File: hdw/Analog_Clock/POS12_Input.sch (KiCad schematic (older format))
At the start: 23 parts

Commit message: a few sch adjustments
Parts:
- removed C?: 0.1uF, Capacitors_SMD:C_0402, symbol Custom_Library:C_Custom
- removed R?: 6.04M, Resistors_SMD:R_0402, symbol Custom_Library:R_Custom
- removed R?: 86.6k, Resistors_SMD:R_0402, symbol Custom_Library:R_Custom
- removed R?: 243k, Resistors_SMD:R_0402, symbol Custom_Library:R_Custom
- removed R?: 100k, Resistors_SMD:R_0402, symbol Custom_Library:R_Custom
- removed R? (x4): 10, Resistors_SMD:R_0402, symbol Custom_Library:R_Custom
- removed R?: 5.1k, Resistors_SMD:R_0402, symbol Custom_Library:R_Custom
- removed R?: 13.7k, Resistors_SMD:R_0402, symbol Custom_Library:R_Custom
- removed R?: 0.02, Resistors_SMD:R_0612, symbol Custom_Library:R_Custom
- removed R?: 5.23k, Resistors_SMD:R_0402, symbol Custom_Library:R_Custom
- removed TP?: TP, Pin_Headers:Pin_Header_Angled_1x01_Pitch2.54mm, symbol Custom_Library:TP
- removed TP? (x2): TP, Custom Footprints Library:Test_Point, symbol Custom_Library:TP
- removed U?: LTC4365DDB, Housings_DFN_QFN:DFN-8-1EP_2x3mm_Pitch0.5mm, symbol Custom_Library:LTC4365DDB
- added C?: 10nF, Capacitors_SMD:C_0603, symbol Custom_Library:C_Custom
- added N?: +12V 1A Power Supply, symbol Mechanical:Housing
- added R?: 6.04k, Resistors_SMD:R_0603, symbol Custom_Library:R_Custom
- added R?: 16.5k, Resistors_SMD:R_0603, symbol Custom_Library:R_Custom
- added R?: 1.15k, Resistors_SMD:R_0603, symbol Custom_Library:R_Custom
- added R?: 51.1k, Resistors_SMD:R_0603, symbol Custom_Library:R_Custom
- added R?: 5.11k, Resistors_SMD:R_0603, symbol Custom_Library:R_Custom
- added R?: 10k, Resistors_SMD:R_0603, symbol Custom_Library:R_Custom
- added R? (x2): R, Resistors_SMD:R_0402, symbol Custom_Library:R_Custom
- added R?: 0.02, Resistors_SMD:R_0612, symbol Custom_Library:R_Custom
- added R? (x2): 10, Resistors_SMD:R_0402, symbol Custom_Library:R_Custom
- added TP? (x2): TP_Pad, Custom Footprints Library:Test_Point, symbol Custom_Library:TP_Pad
- added TP?: TP, Pin_Headers:Pin_Header_Angled_1x01_Pitch2.54mm, symbol Custom_Library:TP
- added U?: TPS26600RHFT, Housings_DFN_QFN:QFN-24-1EP_4x5mm_Pitch0.5mm, symbol Custom_Library:TPS26600RHFT
- C?: footprint Capacitors_SMD:C_0402 -> Capacitors_SMD:C_0603; Digi-Key PN 490-10701-1-ND -> 311-1344-1-ND; display_footprint 0402 -> 0603
- C?: footprint Capacitors_SMD:C_0402 -> Capacitors_SMD:C_0603; Digi-Key PN 490-13295-1-ND -> 1276-1921-1-ND; display_footprint 0402 -> 0603
- C?: footprint Capacitors_SMD:C_0402 -> Capacitors_SMD:C_0603; Digi-Key PN 399-1032-1-ND -> 1276-1018-1-ND; display_footprint 0402 -> 0603
- J?: Digi-Key PN CP-202BH-ND -> (none)
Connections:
- net labels added: POS12_SNS_OUT+, POS12_SNS_OUT-
- net labels removed: POS12_SNS+, POS12_SNS-
- wire segments 70 -> 74
- no-connect marks 0 -> 1
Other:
- note added: "Add EMI filter?"
- note added: "UVLO threshold set to 10.8V\nOVLO threshold set to 13.2V\n\nMODE set to Circuit Breaker with Auto-Retry"
- note removed: "COMBINE FETS"
- note removed: "UVLO threshold set to 10V\nOVLO threshold set to 14V"
- moved on the sheet: C?, D?, J?

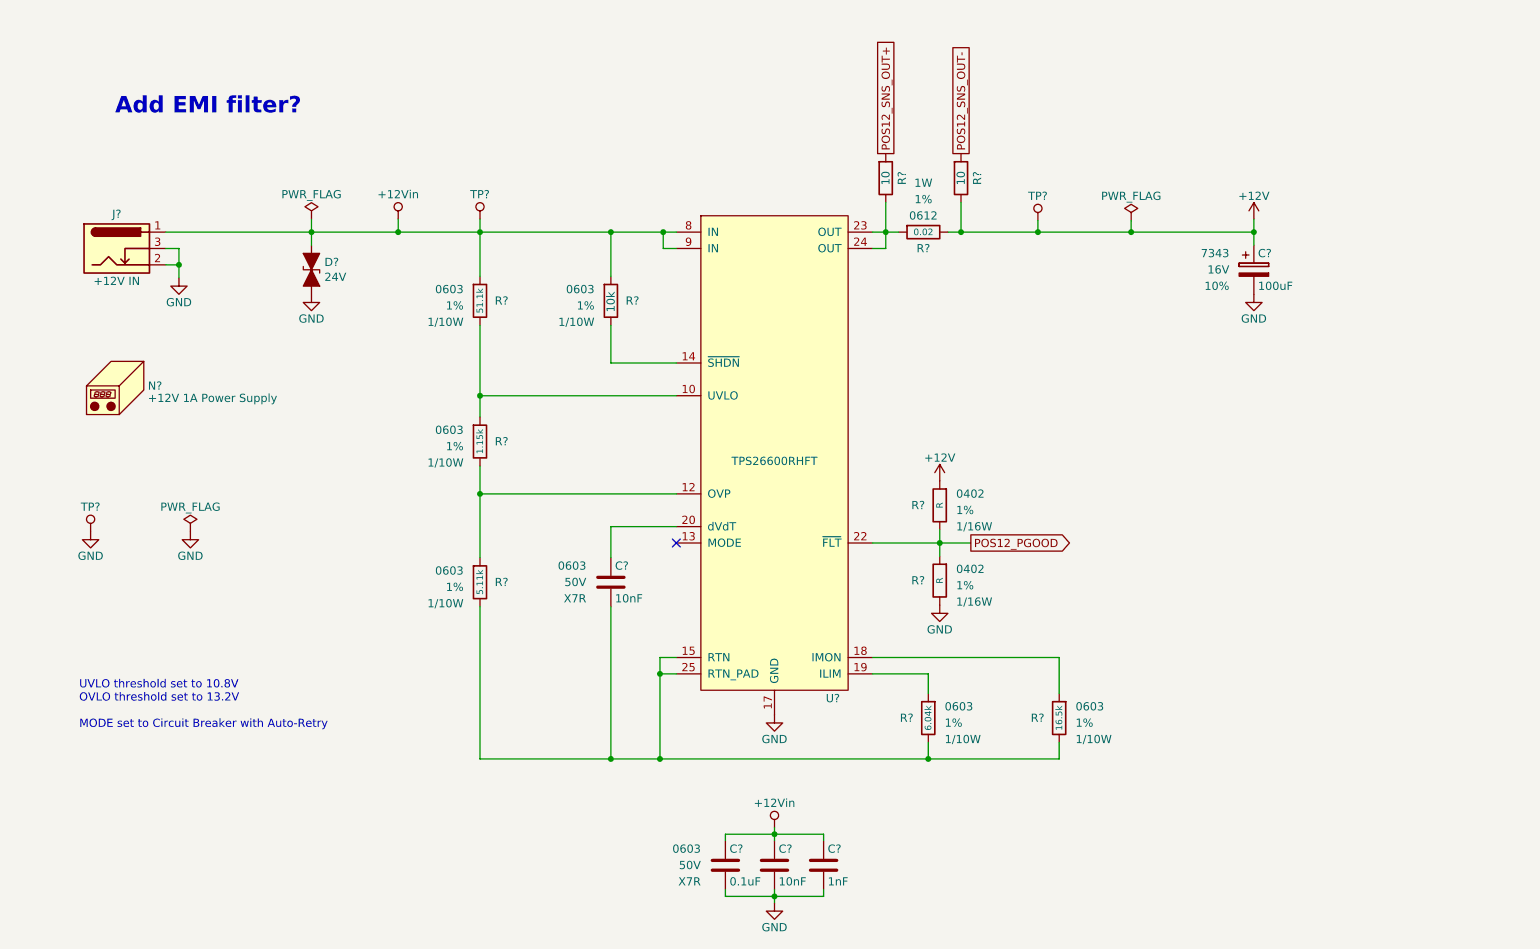
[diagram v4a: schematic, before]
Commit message: Added +20V power supply, updated input power sheet
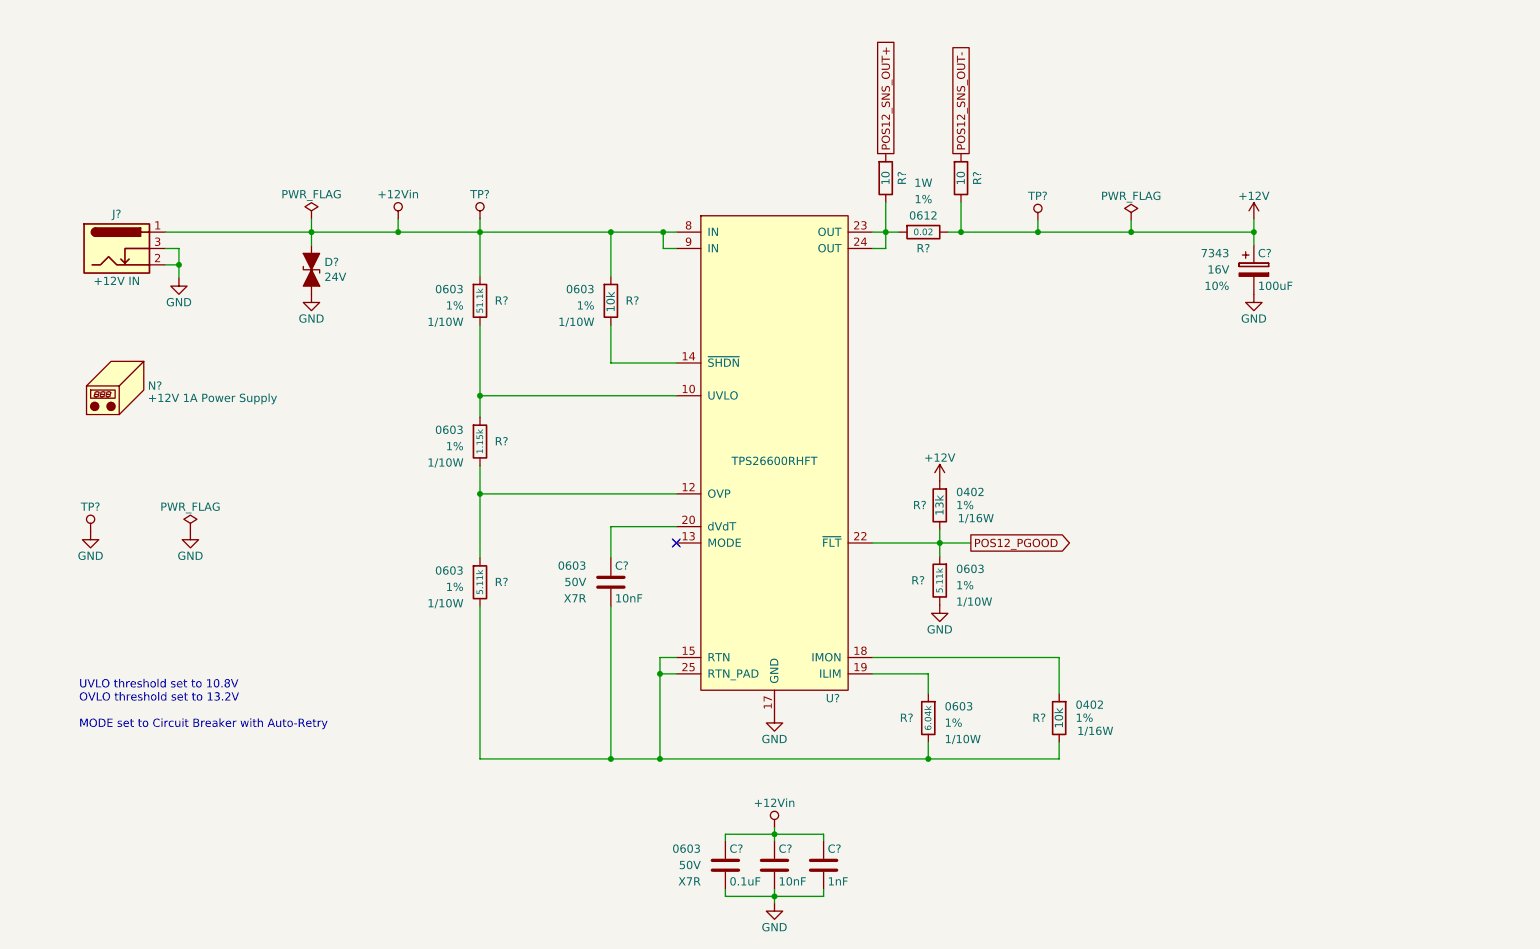
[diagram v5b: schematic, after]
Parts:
- removed R?: 16.5k, Resistors_SMD:R_0603, symbol Custom_Library:R_Custom
- removed R? (x2): R, Resistors_SMD:R_0402, symbol Custom_Library:R_Custom
- added R?: 10k, Resistors_SMD:R_0402, symbol Custom_Library:R_Custom
- added R?: 13k, Resistors_SMD:R_0402, symbol Custom_Library:R_Custom
- added R?: 5.11k, Resistors_SMD:R_0603, symbol Custom_Library:R_Custom
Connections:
- net +12V: now also R?.1
- net GND: now also R?.2
- net POS12_PGOOD: now also R?.1, R?.2
- net at C?.2, R?.2, R?.2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: now also R?.2
- net at U?.18 (IMON): now also R?.1
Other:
- note removed: "Add EMI filter?"
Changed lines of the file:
@@
 Wire Wire Line
 	6540 4940 6200 4940
-$Comp
-L Custom_Library:R_Custom R?
-U 1 1 5DDAEEBB
-P 7340 5210
-AR Path="/5D6B2673/5DDAEEBB" Ref="R?"  Part="1"
-AR Path="/5D6C0D23/5DDAEEBB" Ref="R?"  Part="1"
-AR Path="/5D77A516/5DDAEEBB" Ref="R?"  Part="1"
-AR Path="/5E939CFF/5DDAEEBB" Ref="R?"  Part="1"
-F 0 "R?" H 7250 5210 50  0000 R CNN
-F 1 "16.5k" V 7340 5210 40  0000 C CNN
-F 2 "Resistors_SMD:R_0603" H 7340 5210 50  0001 C CNN
-F 3 "" H 7340 5210 50  0001 C CNN
-F 4 "0603" H 7440 5280 50  0000 L CNN "display_footprint"
-F 5 "1%" H 7440 5180 50  0000 L CNN "Tolerance"
-F 6 "1/10W" H 7440 5080 50  0000 L CNN "Wattage"
-F 7 "RMCF0603FT10K0CT-ND" H 7640 5610 60  0001 C CNN "Digi-Key PN"
-	1    7340 5210
-	1    0    0    -1
-$EndComp
 Wire Wire Line
 	7340 5060 7340 4840
@@
 $EndComp
 $Comp
-L Custom_Library:R_Custom R?
-U 1 1 5F280CDB
-P 6610 3910
-AR Path="/5D6B2673/5F280CDB" Ref="R?"  Part="1"
-AR Path="/5D6C0D23/5F280CDB" Ref="R?"  Part="1"
-AR Path="/5D77A516/5F280CDB" Ref="R?"  Part="1"
-AR Path="/5E939CFF/5F280CDB" Ref="R?"  Part="1"
-F 0 "R?" H 6520 3910 50  0000 R CNN
-F 1 "R" V 6610 3910 40  0000 C CNN
-F 2 "Resistors_SMD:R_0402" H 6610 3910 50  0001 C CNN
-F 3 "" H 6610 3910 50  0001 C CNN
-F 4 "0402" H 6710 3980 50  0000 L CNN "display_footprint"
-F 5 "1%" H 6710 3880 50  0000 L CNN "Tolerance"
-F 6 "1/16W" H 6710 3780 50  0000 L CNN "Wattage"
-	1    6610 3910
-	1    0    0    -1
-$EndComp
-$Comp
-L Custom_Library:R_Custom R?
-U 1 1 5F28228D
-P 6610 4370
-AR Path="/5D6B2673/5F28228D" Ref="R?"  Part="1"
-AR Path="/5D6C0D23/5F28228D" Ref="R?"  Part="1"
-AR Path="/5D77A516/5F28228D" Ref="R?"  Part="1"
-AR Path="/5E939CFF/5F28228D" Ref="R?"  Part="1"
-F 0 "R?" H 6520 4370 50  0000 R CNN
-F 1 "R" V 6610 4370 40  0000 C CNN
-F 2 "Resistors_SMD:R_0402" H 6610 4370 50  0001 C CNN
-F 3 "" H 6610 4370 50  0001 C CNN
-F 4 "0402" H 6710 4440 50  0000 L CNN "display_footprint"
-F 5 "1%" H 6710 4340 50  0000 L CNN "Tolerance"
-F 6 "1/16W" H 6710 4240 50  0000 L CNN "Wattage"
-	1    6610 4370
-	1    0    0    -1
-$EndComp
-$Comp
 L power:GND #PWR?
 U 1 1 5F2844B0
@@
 Wire Wire Line
 	6610 4220 6610 4140
-Text Notes 1570 1530 0    100  ~ 20
-Add EMI filter?
 $Comp
 L Custom_Library:R_Custom R?
@@
 Connection ~ 7780 2240
 Connection ~ 7210 2240
+$Comp
+L Custom_Library:R_Custom R?
+U 1 1 5F2C0F58
+P 7340 5210
+AR Path="/5BB27BA3/5F2C0F58" Ref="R?"  Part="1"
+AR Path="/5BB27BF7/5F2C0F58" Ref="R?"  Part="1"
+AR Path="/5C1DE17A/5F2C0F58" Ref="R?"  Part="1"
+AR Path="/5C1E3A08/5F2C0F58" Ref="R?"  Part="1"
+AR Path="/5D779AE1/5F2C0F58" Ref="R?"  Part="1"
+AR Path="/5CB7718D/5F2C0F58" Ref="R?"  Part="1"
+AR Path="/5E0DC082/5F2C0F58" Ref="R?"  Part="1"
+AR Path="/5E0F263A/5F2C0F58" Ref="R?"  Part="1"
+AR Path="/5E939D31/5F2C0F58" Ref="R?"  Part="1"
+AR Path="/5E98CF45/5F2C0F58" Ref="R?"  Part="1"
+AR Path="/5F280E04/5F2C0F58" Ref="R?"  Part="1"
+AR Path="/5E939CFF/5F2C0F58" Ref="R?"  Part="1"
+F 0 "R?" H 7260 5210 50  0000 R CNN
+F 1 "10k" V 7340 5210 50  0000 C CNN
+F 2 "Resistors_SMD:R_0402" H 7340 5210 50  0001 C CNN
+F 3 "" H 7340 5210 50  0001 C CNN
+F 4 "0402" H 7440 5290 50  0000 L CNN "display_footprint"
+F 5 "1%" H 7440 5210 50  0000 L CNN "Tolerance"
+F 6 "1/16W" H 7450 5130 50  0000 L CNN "Wattage"
+F 7 "RMCF0402FT10K0CT-ND" H 7640 5610 60  0001 C CNN "Digi-Key PN"
+	1    7340 5210
+	1    0    0    -1
+$EndComp
+$Comp
+L Custom_Library:R_Custom R?
+U 1 1 5F2C2BE4
+P 6610 3910
+AR Path="/5BB27BA3/5F2C2BE4" Ref="R?"  Part="1"
+AR Path="/5BB27BF7/5F2C2BE4" Ref="R?"  Part="1"
+AR Path="/5C1DE17A/5F2C2BE4" Ref="R?"  Part="1"
+AR Path="/5C1E3A08/5F2C2BE4" Ref="R?"  Part="1"
+AR Path="/5D779AE1/5F2C2BE4" Ref="R?"  Part="1"
+AR Path="/5CB7718D/5F2C2BE4" Ref="R?"  Part="1"
+AR Path="/5E0DC082/5F2C2BE4" Ref="R?"  Part="1"
+AR Path="/5E0F263A/5F2C2BE4" Ref="R?"  Part="1"
+AR Path="/5E939D31/5F2C2BE4" Ref="R?"  Part="1"
+AR Path="/5E98CF45/5F2C2BE4" Ref="R?"  Part="1"
+AR Path="/5F280E04/5F2C2BE4" Ref="R?"  Part="1"
+AR Path="/5E939CFF/5F2C2BE4" Ref="R?"  Part="1"
+F 0 "R?" H 6530 3910 50  0000 R CNN
+F 1 "13k" V 6610 3910 50  0000 C CNN
+F 2 "Resistors_SMD:R_0402" H 6610 3910 50  0001 C CNN
+F 3 "" H 6610 3910 50  0001 C CNN
+F 4 "0402" H 6710 3990 50  0000 L CNN "display_footprint"
+F 5 "1%" H 6710 3910 50  0000 L CNN "Tolerance"
+F 6 "1/16W" H 6720 3830 50  0000 L CNN "Wattage"
+	1    6610 3910
+	1    0    0    -1
+$EndComp
+$Comp
+L Custom_Library:R_Custom R?
+U 1 1 5F2C6133
+P 6610 4370
+AR Path="/5D6B2673/5F2C6133" Ref="R?"  Part="1"
+AR Path="/5D6C0D23/5F2C6133" Ref="R?"  Part="1"
+AR Path="/5D77A516/5F2C6133" Ref="R?"  Part="1"
+AR Path="/5E939CFF/5F2C6133" Ref="R?"  Part="1"
+F 0 "R?" H 6520 4370 50  0000 R CNN
+F 1 "5.11k" V 6610 4370 40  0000 C CNN
+F 2 "Resistors_SMD:R_0603" H 6610 4370 50  0001 C CNN
+F 3 "" H 6610 4370 50  0001 C CNN
+F 4 "0603" H 6710 4440 50  0000 L CNN "display_footprint"
+F 5 "1%" H 6710 4340 50  0000 L CNN "Tolerance"
+F 6 "1/10W" H 6710 4240 50  0000 L CNN "Wattage"
+F 7 "RMCF0603FT10K0CT-ND" H 6910 4770 60  0001 C CNN "Digi-Key PN"
+	1    6610 4370
+	1    0    0    -1
+$EndComp
 $EndSCHEMATC

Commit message: more analog work, added some more sch stuff
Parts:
- removed R?: 6.04k, Resistors_SMD:R_0603, symbol Custom_Library:R_Custom
- added R?: 10k, Resistors_SMD:R_0402, symbol Custom_Library:R_Custom
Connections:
- net at C?.2, R?.2, R?.2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: now also R?.2
- net at U?.19 (ILIM): now also R?.1
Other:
- note added: "UVLO threshold set to 10.8V\nOVLO threshold set to 13.2V\n\nMODE set to Circuit Breaker with Auto-Retry\n\nOutput Current Limit set to 1.2A"
- note removed: "UVLO threshold set to 10.8V\nOVLO threshold set to 13.2V\n\nMODE set to Circuit Breaker with Auto-Retry"
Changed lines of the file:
@@
 $Descr A 11000 8500
 encoding utf-8
-Sheet 2 23
+Sheet 2 24
 Title "Incrementor"
 Date "2019-09-03"
@@
 	2770 2320 2770 2240
 Text Notes 1350 5280 0    50   ~ 0
-UVLO threshold set to 10.8V\nOVLO threshold set to 13.2V\n\nMODE set to Circuit Breaker with Auto-Retry
+UVLO threshold set to 10.8V\nOVLO threshold set to 13.2V\n\nMODE set to Circuit Breaker with Auto-Retry\n\nOutput Current Limit set to 1.2A
 $Comp
 L power:PWR_FLAG #FLG?
@@
 Wire Wire Line
 	6200 4140 6610 4140
-$Comp
-L Custom_Library:R_Custom R?
-U 1 1 5DDA6EDA
-P 6540 5210
-AR Path="/5D6B2673/5DDA6EDA" Ref="R?"  Part="1"
-AR Path="/5D6C0D23/5DDA6EDA" Ref="R?"  Part="1"
-AR Path="/5D77A516/5DDA6EDA" Ref="R?"  Part="1"
-AR Path="/5E939CFF/5DDA6EDA" Ref="R?"  Part="1"
-F 0 "R?" H 6450 5210 50  0000 R CNN
-F 1 "6.04k" V 6540 5210 40  0000 C CNN
-F 2 "Resistors_SMD:R_0603" H 6540 5210 50  0001 C CNN
-F 3 "" H 6540 5210 50  0001 C CNN
-F 4 "0603" H 6640 5280 50  0000 L CNN "display_footprint"
-F 5 "1%" H 6640 5180 50  0000 L CNN "Tolerance"
-F 6 "1/10W" H 6640 5080 50  0000 L CNN "Wattage"
-F 7 "RMCF0603FT10K0CT-ND" H 6840 5610 60  0001 C CNN "Digi-Key PN"
-	1    6540 5210
-	1    0    0    -1
-$EndComp
 Wire Wire Line
 	6540 5060 6540 4940
@@
 	1    0    0    -1
 $EndComp
+$Comp
+L Custom_Library:R_Custom R?
+U 1 1 5F374B48
+P 6540 5210
+AR Path="/5BB27BA3/5F374B48" Ref="R?"  Part="1"
+AR Path="/5BB27BF7/5F374B48" Ref="R?"  Part="1"
+AR Path="/5C1DE17A/5F374B48" Ref="R?"  Part="1"
+AR Path="/5C1E3A08/5F374B48" Ref="R?"  Part="1"
+AR Path="/5D779AE1/5F374B48" Ref="R?"  Part="1"
+AR Path="/5CB7718D/5F374B48" Ref="R?"  Part="1"
+AR Path="/5E0DC082/5F374B48" Ref="R?"  Part="1"
+AR Path="/5E0F263A/5F374B48" Ref="R?"  Part="1"
+AR Path="/5E939D31/5F374B48" Ref="R?"  Part="1"
+AR Path="/5E98CF45/5F374B48" Ref="R?"  Part="1"
+AR Path="/5F280E04/5F374B48" Ref="R?"  Part="1"
+AR Path="/5E939CFF/5F374B48" Ref="R?"  Part="1"
+F 0 "R?" H 6460 5210 50  0000 R CNN
+F 1 "10k" V 6540 5210 50  0000 C CNN
+F 2 "Resistors_SMD:R_0402" H 6540 5210 50  0001 C CNN
+F 3 "" H 6540 5210 50  0001 C CNN
+F 4 "0402" H 6640 5290 50  0000 L CNN "display_footprint"
+F 5 "1%" H 6640 5210 50  0000 L CNN "Tolerance"
+F 6 "1/16W" H 6650 5130 50  0000 L CNN "Wattage"
+F 7 "RMCF0402FT10K0CT-ND" H 6840 5610 60  0001 C CNN "Digi-Key PN"
+	1    6540 5210
+	1    0    0    -1
+$EndComp

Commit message: big sch push
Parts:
- C201, C203: renamed from C?; Digi-Key PN 1276-1921-1-ND -> 399-7842-1-ND
- C202: renamed from C?; Digi-Key PN 311-1344-1-ND -> 399-7845-1-ND
- C204: renamed from C?; Digi-Key PN 1276-1018-1-ND -> 399-1083-1-ND
- R201, R202, R203, R204, R209: renamed from R?; Digi-Key PN RMCF0603FT10K0CT-ND -> (none)
- R205, R210: renamed from R?; footprint Resistors_SMD:R_0402 -> Resistors_SMD:R_0603; Digi-Key PN 541-3964-1-ND -> (none); Wattage 1/16W -> 1/10W; display_footprint 0402 -> 0603
- R207, R211: renamed from R?; footprint Resistors_SMD:R_0402 -> Resistors_SMD:R_0603; Digi-Key PN RMCF0402FT10K0CT-ND -> (none); Wattage 1/16W -> 1/10W; display_footprint 0402 -> 0603
- R208: renamed from R?; footprint Resistors_SMD:R_0402 -> Resistors_SMD:R_0603; Wattage 1/16W -> 1/10W; display_footprint 0402 -> 0603
- TP201: renamed from TP?; Digi-Key PN 36-5005-ND -> (none)
- gave numbers to parts that had none: 8
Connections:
- net POS12_SNS_OUT+ renamed POS12_SNS+
- net POS12_SNS_OUT- renamed POS12_SNS-
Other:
- note added: "+3.3V Logic Level"

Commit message: Much more schematic progress
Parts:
- R201: Digi-Key PN (none) -> RMCF0603FT51K1TR-ND
- R202: Digi-Key PN (none) -> RMCF0603FT1K15CT-ND
- R203, R209: Digi-Key PN (none) -> CR0603-FX-5111ELFCT-ND
- R204, R205, R207, R210, R211: Digi-Key PN (none) -> YAG2321CT-ND
- R208: Digi-Key PN (none) -> 311-13.0KHRCT-ND
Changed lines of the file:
@@
 encoding utf-8
 Sheet 2 25
-Title "Incrementor"
-Date "2019-09-03"
+Title "Analog Clock"
+Date "2020-08-15"
 Rev "A"
 Comp "Drew Maatman"
@@
 F 5 "1%" H 3900 3490 50  0000 L CNN "Tolerance"
 F 6 "1/10W" H 3900 3390 50  0000 L CNN "Wattage"
-F 7 "" H 4100 3920 60  0001 C CNN "Digi-Key PN"
+F 7 "RMCF0603FT1K15CT-ND" H 4100 3920 60  0001 C CNN "Digi-Key PN"
 	1    3800 3520
 	-1   0    0    -1
@@
 F 5 "1%" H 3900 2630 50  0000 L CNN "Tolerance"
 F 6 "1/10W" H 3900 2530 50  0000 L CNN "Wattage"
-F 7 "" H 4100 3060 60  0001 C CNN "Digi-Key PN"
+F 7 "RMCF0603FT51K1TR-ND" H 4100 3060 60  0001 C CNN "Digi-Key PN"
 	1    3800 2660
 	-1   0    0    -1
@@
 F 5 "1%" H 3900 4350 50  0000 L CNN "Tolerance"
 F 6 "1/10W" H 3900 4250 50  0000 L CNN "Wattage"
-F 7 "" H 4100 4780 60  0001 C CNN "Digi-Key PN"
+F 7 "CR0603-FX-5111ELFCT-ND" H 4100 4780 60  0001 C CNN "Digi-Key PN"
 	1    3800 4380
 	-1   0    0    -1
@@
 F 5 "1%" H 4700 2630 50  0000 L CNN "Tolerance"
 F 6 "1/10W" H 4700 2530 50  0000 L CNN "Wattage"
-F 7 "" H 4900 3060 60  0001 C CNN "Digi-Key PN"
+F 7 "YAG2321CT-ND" H 4900 3060 60  0001 C CNN "Digi-Key PN"
 	1    4600 2660
 	-1   0    0    -1
@@
 F 5 "1%" V 6480 1910 50  0001 C CNN "Tolerance"
 F 6 "1/10W" V 6580 1910 50  0001 C CNN "Wattage"
-F 7 "" H 6280 1910 50  0001 C CNN "Digi-Key PN"
+F 7 "YAG2321CT-ND" H 6280 1910 50  0001 C CNN "Digi-Key PN"
 	1    6280 1910
 	-1   0    0    -1
@@
 F 5 "1%" V 6940 1910 50  0001 C CNN "Tolerance"
 F 6 "1/10W" V 7040 1910 50  0001 C CNN "Wattage"
-F 7 "" H 6740 1910 50  0001 C CNN "Digi-Key PN"
+F 7 "YAG2321CT-ND" H 6740 1910 50  0001 C CNN "Digi-Key PN"
 	1    6740 1910
 	-1   0    0    -1
@@
 F 5 "1%" H 7440 5210 50  0000 L CNN "Tolerance"
 F 6 "1/10W" H 7450 5130 50  0000 L CNN "Wattage"
-F 7 "" H 7640 5610 60  0001 C CNN "Digi-Key PN"
+F 7 "YAG2321CT-ND" H 7640 5610 60  0001 C CNN "Digi-Key PN"
 	1    7340 5210
 	1    0    0    -1
@@
 F 5 "1%" H 6710 3910 50  0000 L CNN "Tolerance"
 F 6 "1/10W" H 6720 3830 50  0000 L CNN "Wattage"
+F 7 "311-13.0KHRCT-ND" H 6610 3910 50  0001 C CNN "Digi-Key PN"
 	1    6610 3910
 	1    0    0    -1
@@
 F 5 "1%" H 6710 4340 50  0000 L CNN "Tolerance"
 F 6 "1/10W" H 6710 4240 50  0000 L CNN "Wattage"
-F 7 "" H 6910 4770 60  0001 C CNN "Digi-Key PN"
+F 7 "CR0603-FX-5111ELFCT-ND" H 6910 4770 60  0001 C CNN "Digi-Key PN"
 	1    6610 4370
 	1    0    0    -1
@@
 F 5 "1%" H 6640 5210 50  0000 L CNN "Tolerance"
 F 6 "1/10W" H 6650 5130 50  0000 L CNN "Wattage"
-F 7 "" H 6840 5610 60  0001 C CNN "Digi-Key PN"
+F 7 "YAG2321CT-ND" H 6840 5610 60  0001 C CNN "Digi-Key PN"
 	1    6540 5210
 	1    0    0    -1
